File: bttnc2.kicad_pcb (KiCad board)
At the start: 2 copper layers, 70 x 40 mm, 105 parts, among them K1 MK12C02, P1 ISP, P2 BATTERY, P3 BNC, P4 USB_OTG, P5 BNC, P6 CONN_01X03, Q1 MMBT3904, SW1 SW_PUSH, U1 HC-05, U10 Quectel-L80, U11 FDG6342L, U2 APE8800N, U3 BU33TD3WG, U4 ATMEGA328P-AU, U5 DRA818V, U6 DW01-P, U7 TP4056, U8 8205A, U9 LM358, X1 QKT-3225SMD 16.0000MHz

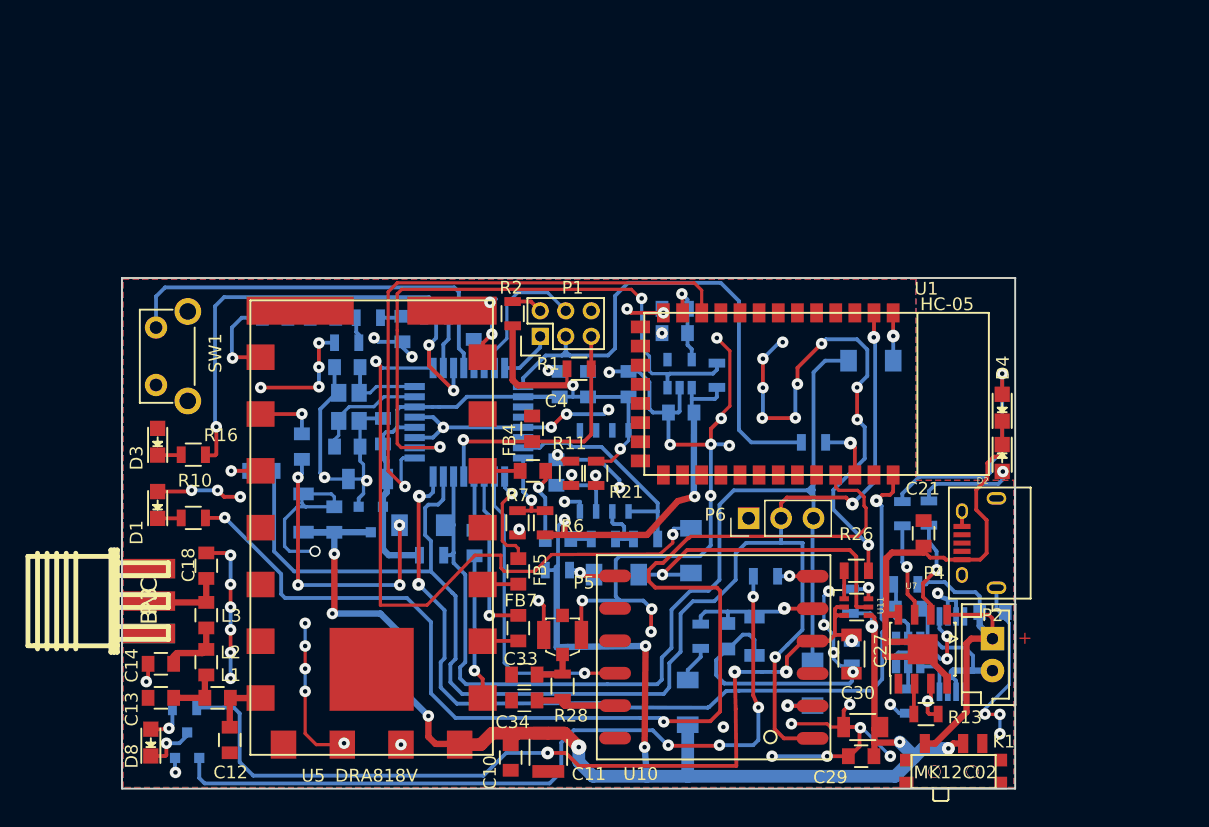
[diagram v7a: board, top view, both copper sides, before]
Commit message: Update and rearrange labels
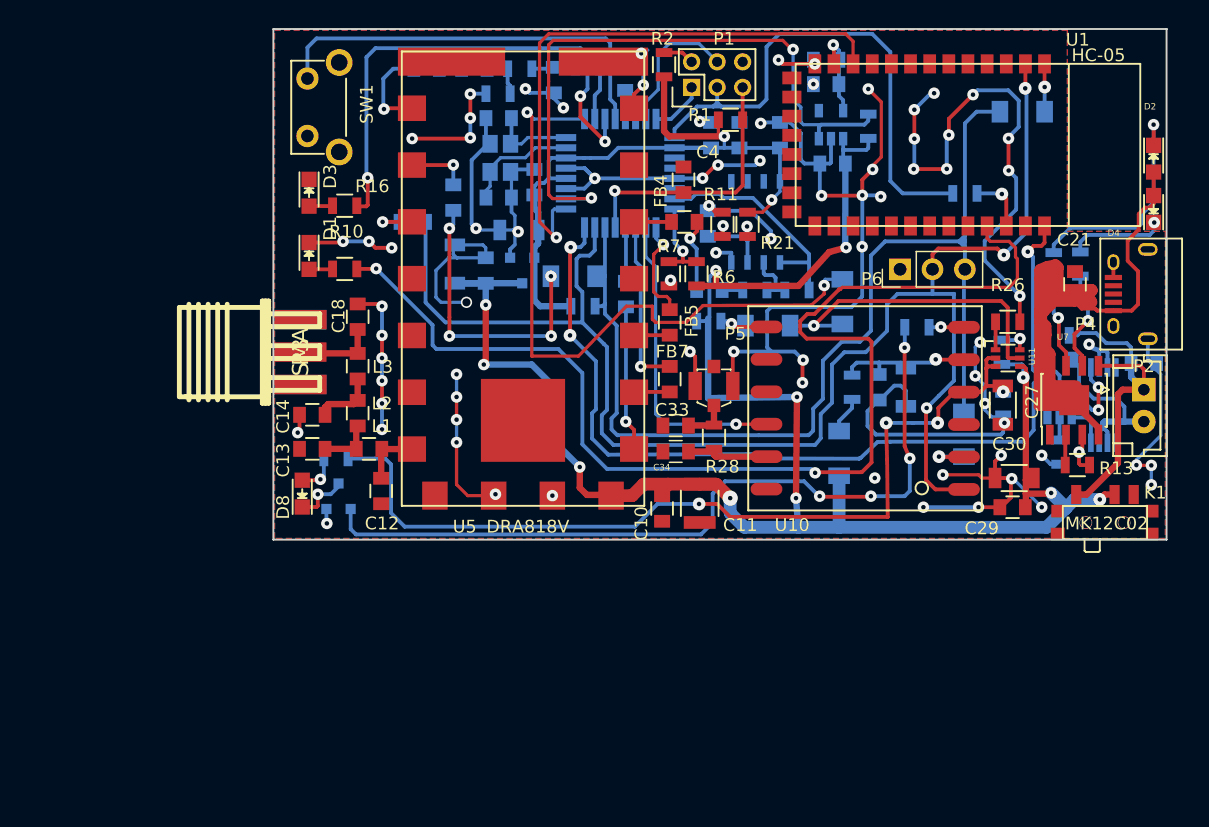
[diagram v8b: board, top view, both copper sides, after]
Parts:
- D1: value LED -> Blue LED
- P3: value BNC -> SMA
- P5: value BNC -> U.FL
- P6: value CONN_01X03 -> Serial
- moved C17 22.8 mm to (156.9, 92.3)
- moved FB8 22.8 mm to (140.7, 102.5)
- moved P5 22.8 mm to (147.6, 109.7)
- moved R14 22.8 mm to (174.7, 114.9)
- moved R2 22.8 mm to (143.7, 84.5)
- moved U4 22.8 mm to (140.3, 93.0)
- moved U6 22.8 mm to (174.7, 111.0)
- moved C6 22.8 mm to (130.7, 94.9)
- moved FB2 22.8 mm to (127.2, 94.9)
- moved L2 22.8 mm to (119.7, 111.8)
- moved L3 22.8 mm to (119.7, 108.1)
- moved Q1 22.8 mm to (118.2, 118.3)
- moved R23 22.8 mm to (118.0, 115.3)
- moved C1 22.8 mm to (147.4, 90.0)
- moved C16 22.8 mm to (129.7, 100.6)
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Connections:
- D1 pad 1: Net-(D1-Pad1) -> GND
- D1 pad 2: GND -> Net-(D1-Pad2)
- D2 pad 1: Net-(C21-Pad1) -> Net-(D2-Pad1)
- D2 pad 2: Net-(D2-Pad2) -> Net-(C21-Pad1)
- D3 pad 1: Net-(D3-Pad1) -> GND
- D3 pad 2: GND -> Net-(D3-Pad2)
- D4 pad 1: Net-(C21-Pad1) -> Net-(D4-Pad1)
- D4 pad 2: Net-(D4-Pad2) -> Net-(C21-Pad1)
- R10 pad 2: Net-(D1-Pad1) -> Net-(D1-Pad2)
- R16 pad 2: Net-(D3-Pad1) -> Net-(D3-Pad2)
- R17 pad 1: Net-(D2-Pad2) -> Net-(D2-Pad1)
- R18 pad 2: Net-(D4-Pad2) -> Net-(D4-Pad1)
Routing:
- net Net-(C21-Pad1): track 40.7 -> 78.1 mm
- net Net-(D4-Pad2): track 17.9 -> 0.00 mm, vias 1 -> 0
- net Net-(D4-Pad1): track 0.00 -> 17.9 mm, vias 0 -> 1
- net Net-(D2-Pad1): track 0.00 -> 7.61 mm, vias 0 -> 1
- net Net-(D2-Pad2): track 7.61 -> 0.00 mm, vias 1 -> 0
- net Net-(D3-Pad2): track 0.00 -> 1.86 mm
- net Net-(D3-Pad1): track 1.86 -> 0.00 mm
- net Net-(D1-Pad2): track 0.00 -> 1.86 mm
- net Net-(D1-Pad1): track 1.86 -> 0.00 mm
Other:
- board text added: "-"
